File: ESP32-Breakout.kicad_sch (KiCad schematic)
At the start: 3 parts, among them U1 ESP32-S2-DevKitC-1

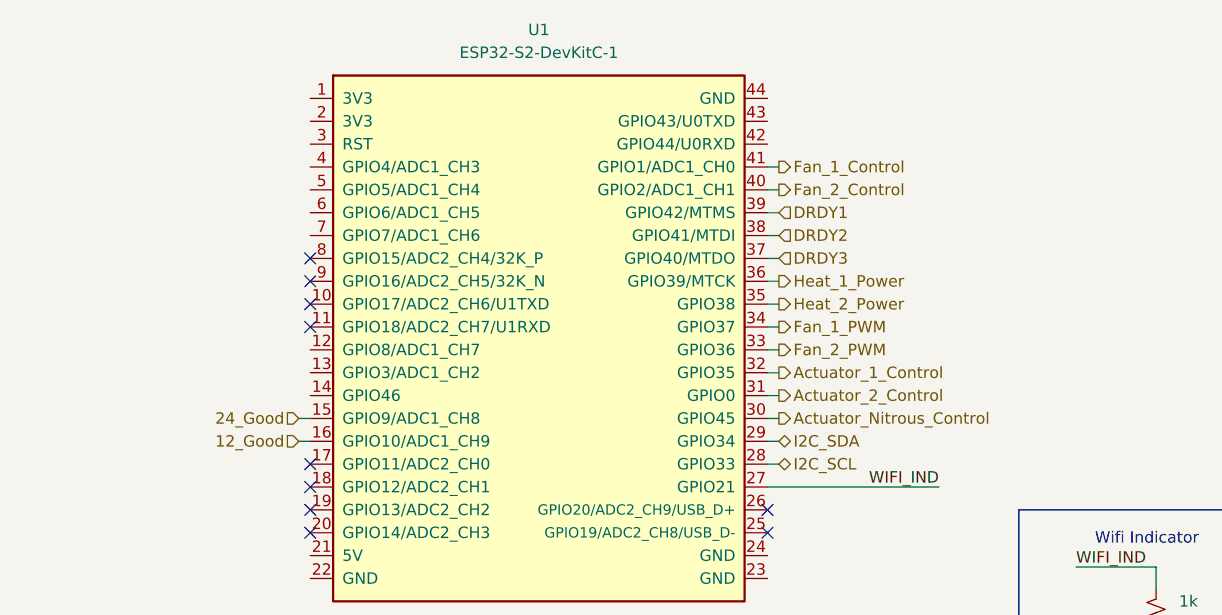
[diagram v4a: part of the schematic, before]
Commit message: Initial PCB placement and wiring.
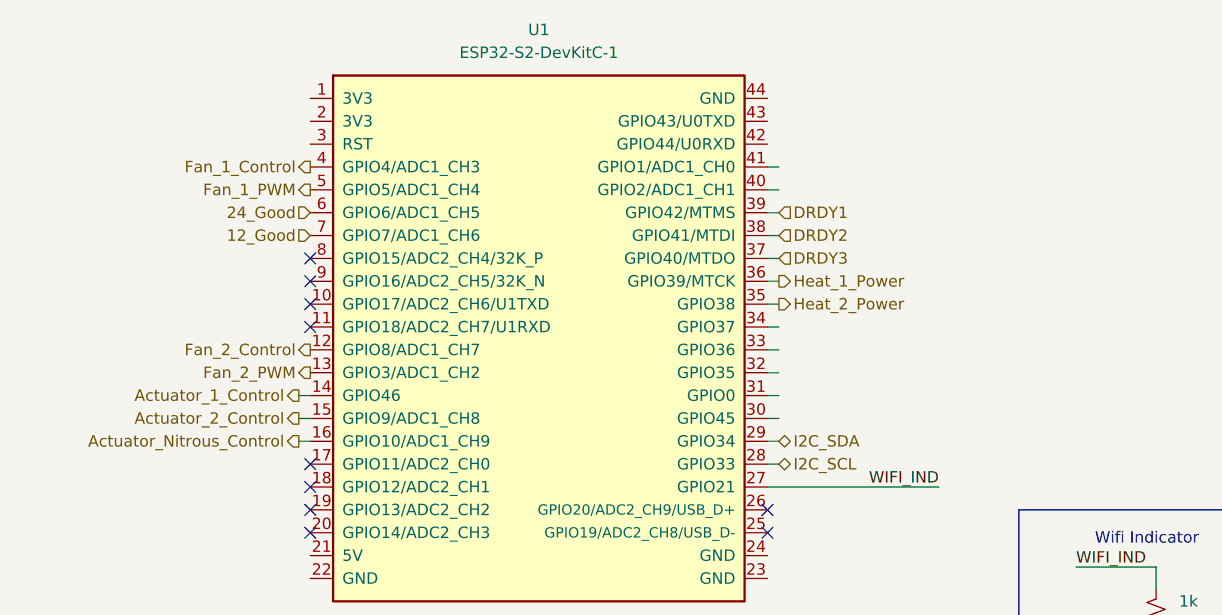
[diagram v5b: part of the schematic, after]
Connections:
- net 12_Good: now also U1.7 (GPIO7/ADC1_CH6); no longer U1.16 (GPIO10/ADC1_CH9)
- net 24_Good: now also U1.6 (GPIO6/ADC1_CH5); no longer U1.15 (GPIO9/ADC1_CH8)
- net Actuator_1_Control: now also U1.14 (GPIO46); no longer U1.32 (GPIO35)
- net Actuator_2_Control: now also U1.15 (GPIO9/ADC1_CH8); no longer U1.31 (GPIO0)
- net Actuator_Nitrous_Control: now also U1.16 (GPIO10/ADC1_CH9); no longer U1.30 (GPIO45)
- net Fan_1_Control: now also U1.4 (GPIO4/ADC1_CH3); no longer U1.41 (GPIO1/ADC1_CH0)
- net Fan_1_PWM: now also U1.5 (GPIO5/ADC1_CH4); no longer U1.34 (GPIO37)
- net Fan_2_Control: now also U1.12 (GPIO8/ADC1_CH7); no longer U1.40 (GPIO2/ADC1_CH1)
- net Fan_2_PWM: now also U1.13 (GPIO3/ADC1_CH2); no longer U1.33 (GPIO36)
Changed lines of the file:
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@@
+	(wire
+		(pts
+			(xy 80.01 72.39) (xy 81.28 72.39)
+		)
+		(stroke
+			(width 0)
+			(type default)
+		)
+	)
 	(wire
 		(pts
@@
 		)
 	)
+	(hierarchical_label "DRDY2"
+		(shape input)
+		(at 133.35 54.61 0)
+		(effects
+			(font
+				(size 1.27 1.27)
+			)
+			(justify left)
+		)
+	)
+	(hierarchical_label "Heat_1_Power"
+		(shape output)
+		(at 133.35 59.69 0)
+		(effects
+			(font
+				(size 1.27 1.27)
+			)
+			(justify left)
+		)
+	)
+	(hierarchical_label "Actuator_Nitrous_Control"
+		(shape output)
+		(at 80.01 77.47 180)
+		(effects
+			(font
+				(size 1.27 1.27)
+			)
+			(justify right)
+		)
+	)
+	(hierarchical_label "Heat_2_Power"
+		(shape output)
+		(at 133.35 62.23 0)
+		(effects
+			(font
+				(size 1.27 1.27)
+			)
+			(justify left)
+		)
+	)
+	(hierarchical_label "Fan_1_Control"
+		(shape output)
+		(at 81.28 46.99 180)
+		(effects
+			(font
+				(size 1.27 1.27)
+			)
+			(justify right)
+		)
+	)
 	(hierarchical_label "Actuator_2_Control"
 		(shape output)
-		(at 133.35 72.39 0)
-		(effects
-			(font
-				(size 1.27 1.27)
-			)
-			(justify left)
-		)
-	)
-	(hierarchical_label "Fan_2_Control"
-		(shape output)
-		(at 133.35 49.53 0)
-		(effects
-			(font
-				(size 1.27 1.27)
-			)
-			(justify left)
-		)
-	)
-	(hierarchical_label "Actuator_1_Control"
-		(shape output)
-		(at 133.35 69.85 0)
-		(effects
-			(font
-				(size 1.27 1.27)
-			)
-			(justify left)
-		)
-	)
-	(hierarchical_label "DRDY2"
-		(shape input)
-		(at 133.35 54.61 0)
-		(effects
-			(font
-				(size 1.27 1.27)
-			)
-			(justify left)
-		)
-	)
-	(hierarchical_label "Heat_1_Power"
-		(shape output)
-		(at 133.35 59.69 0)
-		(effects
-			(font
-				(size 1.27 1.27)
-			)
-			(justify left)
-		)
-	)
-	(hierarchical_label "Fan_2_PWM"
-		(shape output)
-		(at 133.35 67.31 0)
-		(effects
-			(font
-				(size 1.27 1.27)
-			)
-			(justify left)
-		)
-	)
-	(hierarchical_label "24_Good"
-		(shape input)
 		(at 80.01 74.93 180)
 		(effects
@@
 			)
 			(justify right)
-		)
-	)
-	(hierarchical_label "Heat_2_Power"
-		(shape output)
-		(at 133.35 62.23 0)
-		(effects
-			(font
-				(size 1.27 1.27)
-			)
-			(justify left)
-		)
-	)
-	(hierarchical_label "Fan_1_PWM"
-		(shape output)
-		(at 133.35 64.77 0)
-		(effects
-			(font
-				(size 1.27 1.27)
-			)
-			(justify left)
-		)
-	)
-	(hierarchical_label "12_Good"
-		(shape input)
-		(at 80.01 77.47 180)
-		(effects
-			(font
-				(size 1.27 1.27)
-			)
-			(justify right)
-		)
-	)
-	(hierarchical_label "Actuator_Nitrous_Control"
-		(shape output)
-		(at 133.35 74.93 0)
-		(effects
-			(font
-				(size 1.27 1.27)
-			)
-			(justify left)
 		)
 	)
@@
 		)
 	)
+	(hierarchical_label "24_Good"
+		(shape input)
+		(at 81.28 52.07 180)
+		(effects
+			(font
+				(size 1.27 1.27)
+			)
+			(justify right)
+		)
+	)
+	(hierarchical_label "12_Good"
+		(shape input)
+		(at 81.28 54.61 180)
+		(effects
+			(font
+				(size 1.27 1.27)
+			)
+			(justify right)
+		)
+	)
 	(hierarchical_label "DRDY1"
 		(shape input)
@@
 			)
 			(justify left)
+		)
+	)
+	(hierarchical_label "Fan_1_PWM"
+		(shape output)
+		(at 81.28 49.53 180)
+		(effects
+			(font
+				(size 1.27 1.27)
+			)
+			(justify right)
+		)
+	)
+	(hierarchical_label "Fan_2_Control"
+		(shape output)
+		(at 81.28 67.31 180)
+		(effects
+			(font
+				(size 1.27 1.27)
+			)
+			(justify right)
+		)
+	)
+	(hierarchical_label "Actuator_1_Control"
+		(shape output)
+		(at 80.01 72.39 180)
+		(effects
+			(font
+				(size 1.27 1.27)
+			)
+			(justify right)
 		)
 	)
@@
 		)
 	)
-	(hierarchical_label "Fan_1_Control"
-		(shape output)
-		(at 133.35 46.99 0)
-		(effects
-			(font
-				(size 1.27 1.27)
-			)
-			(justify left)
-		)
-	)
+	(hierarchical_label "Fan_2_PWM"
+		(shape output)
+		(at 81.28 69.85 180)
+		(effects
+			(font
+				(size 1.27 1.27)
+			)
+			(justify right)
+		)
+	)
